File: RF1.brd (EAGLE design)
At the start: 49.5 x 49.6 mm, 15 parts, among them J1 5v, Q1 16mhz, U1 ATMEGA328P_PDIP

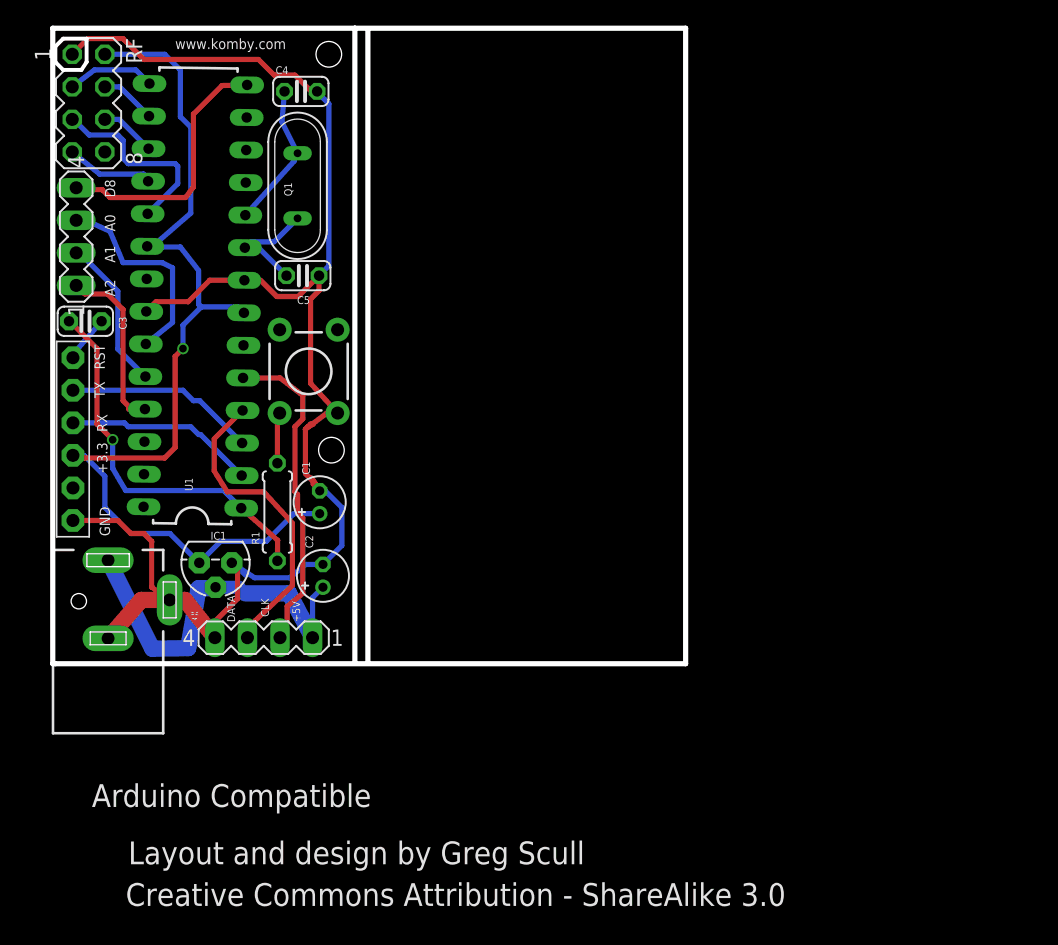
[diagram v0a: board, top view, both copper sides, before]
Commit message: Updated Revised layout of RF1 board
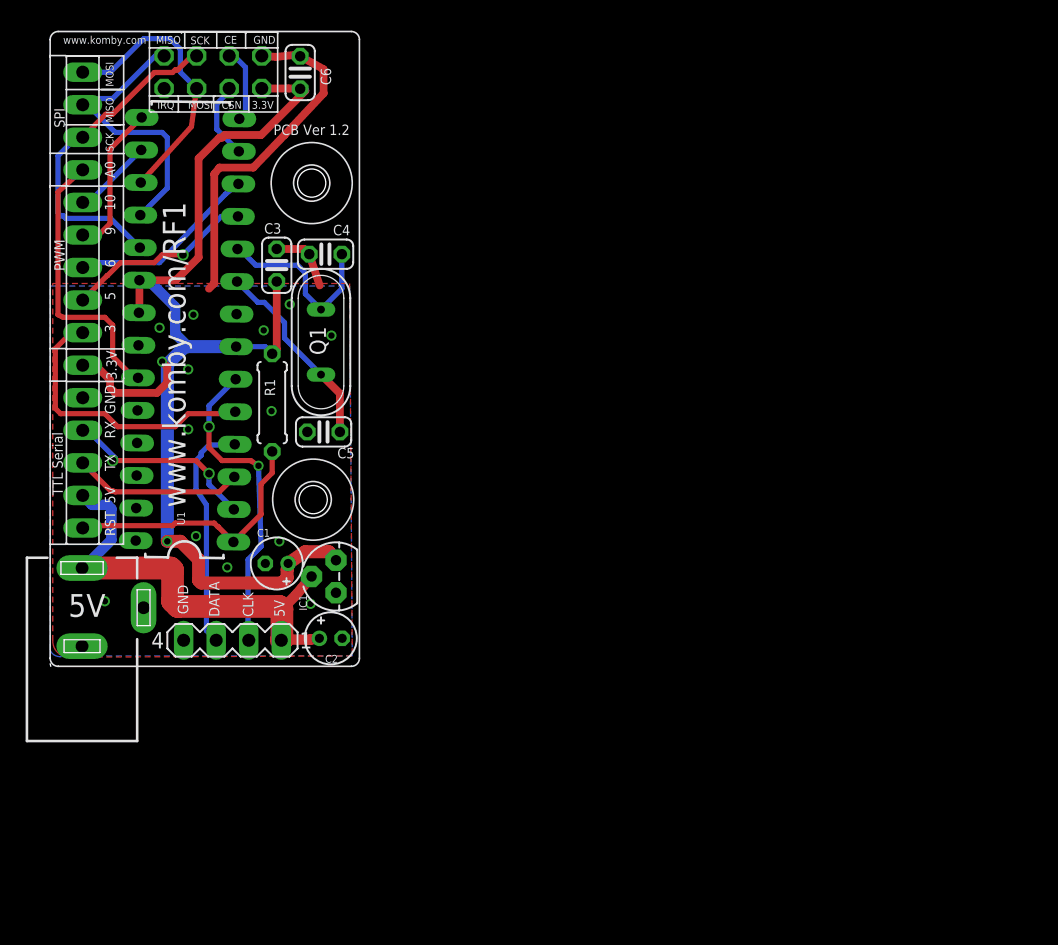
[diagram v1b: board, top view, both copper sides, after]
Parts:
- removed JP1: (no value), adafruit:1X06-BIG
- removed RF: (no value), con-lstb:MA04-2
- removed S1: (no value), SparkFun-Electromechanical:TACTILE-PTH
- removed SV2: (no value), con-lstb:MA04-1
- added C6: 100n, resistor:C025-024X044
- added U$3: RF1_5CMX2.5CM_SHEILD, komby1:KOMBY_RF1_SHEILD_5X2.5
- C3: value .1uf -> 100n; device adafruit:C025-024X044 -> resistor:C025-024X044
- moved C3 15.6 mm to (17.7, 31.3), turned to 90 degrees
- moved C4 12.8 mm to (21.5, 32.2), turned to 180 degrees
- moved Q1 12.3 mm to (21.1, 25.3)
- moved C5 12.3 mm to (21.3, 18.3), turned to 180 degrees
- moved IC1 9.46 mm to (22.3, 7.01), turned to 90 degrees
- moved R1 8.54 mm to (17.3, 20.6)
- moved C1 5.83 mm to (17.7, 8.03), turned to 180 degrees
- moved C2 4.91 mm to (21.9, 2.18), turned to 0 degrees
- moved U1 2.71 mm to (10.7, 26.3)
- moved SV1 2.45 mm to (14.2, 2.03)
- moved J1 2.12 mm to (2.49, 4.57)
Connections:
- removed net 3.3V: C1.+, IC1.3, JP1.4, RF.2, U1.20, U1.7
- removed net ADC0: SV2.3, U1.23
- removed net ADC1: SV2.2, U1.24
- removed net ADC2: SV2.1, U1.25
- removed net CE: RF.3, U1.15
- removed net CSN: RF.4, U1.16
- removed net IRQ: RF.8
- removed net N$1: R1.2, S1.4
- removed net N$7: C3.2, JP1.1
- removed net N$8: JP1.5
- removed net PB0: SV2.4, U1.14
- new net +3V3: C1.+, C3.1, C6.2, IC1.3, R1.2, U$3.3.3V, U$3.RF_3.3V, U1.20, U1.21, U1.7
- new net PC0: U$3.A0, U1.23
- new net PC1: U1.24
- new net PC2: U1.25
- new net PC3: U1.26
- new net PWM1_D3: U$3.PWM1_D3, U1.5
- new net PWM2_D5: U$3.PWM2_D5, U1.11
- new net PWM3_D6: U$3.PWM3_D6, U1.12
- new net PWM4_D9: U$3.PWM4_D9, U1.15
- new net PWM5_D10: U$3.PWM5_D10, U1.16
- new net RF_CE: U$3.RF_CE, U1.14
- new net RF_CSN: U$3.RF_CSN, U1.13
- net +5V: now also U$3.5V
- net GND: now also C3.2, C6.1, U$3.GND, U$3.RF_GND; no longer JP1.6, RF.1, S1.2
- net MISO: now also U$3.MISO, U$3.RF_MISO; no longer RF.7
- net MOSI: now also U$3.MOSI, U$3.RF_MOSI; no longer RF.6
- net PCLK: now also U1.6; no longer U1.5
- net RESET: now also U$3.RESET; no longer C3.1
- net RX: now also U$3.RX; no longer JP1.3
- net SCK: now also U$3.RF_SCK, U$3.SCK; no longer RF.5
- net TX: now also U$3.TX; no longer JP1.2
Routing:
- net +3V3: track 0.00 -> 93.4 mm, vias 0 -> 2
- net GND: track 122.5 -> 32.8 mm, vias 0 -> 13
- net 3.3V: track 79.3 -> 0.00 mm, vias 1 -> 0
- net PWM1_D3: track 0.00 -> 22.4 mm
- net PC0: track 0.00 -> 21.8 mm
- net PB0: track 20.7 -> 0.00 mm
- net MOSI: track 4.36 -> 21.5 mm
- net ADC0: track 16.4 -> 0.00 mm
- net MISO: track 6.83 -> 22.5 mm
- net PWM3_D6: track 0.00 -> 14.9 mm
- net PWM2_D5: track 0.00 -> 14.8 mm, vias 0 -> 1
- net ADC2: track 13.6 -> 0.00 mm
- net ADC1: track 12.0 -> 0.00 mm
- net PWM4_D9: track 0.00 -> 11.8 mm
- net SCK: track 15.3 -> 26.0 mm
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- added copper zone on layer 1, net GND
- added copper zone on layer 16, net GND
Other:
- board size 49.5 x 49.6 mm -> 7 x 7.1 mm
- board text added: "5V"
- board text added: "PCB Ver 1.2"
- board text removed: "+3.3"
- board text removed: "+5V"
- board text removed: "A0"
- board text removed: "A1"
- board text removed: "A2"
- board text removed: "Arduino Compatible"
- board text removed: "Creative Commons Attribution - ShareAlike 3.0"
- board text removed: "D8"
- board text removed: "Layout and design by Greg Scull"
- board text removed: "RST"
- board text removed: "RX"
- board text removed: "TX"
